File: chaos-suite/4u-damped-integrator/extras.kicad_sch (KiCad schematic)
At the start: 15 parts

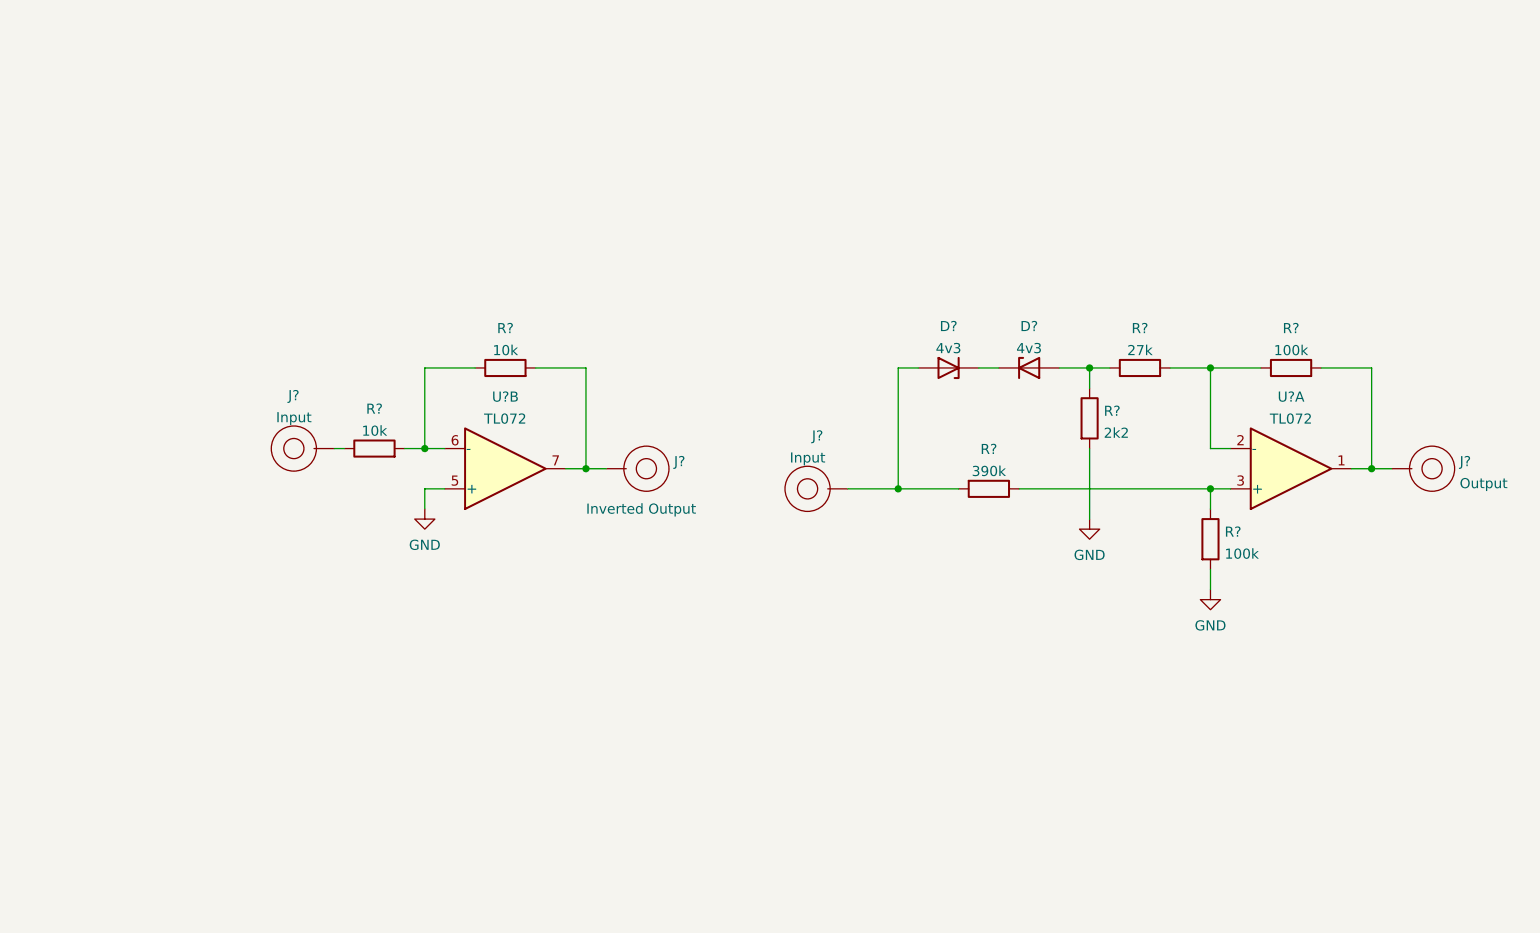
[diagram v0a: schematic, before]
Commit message: Laying out damped integrator pcb
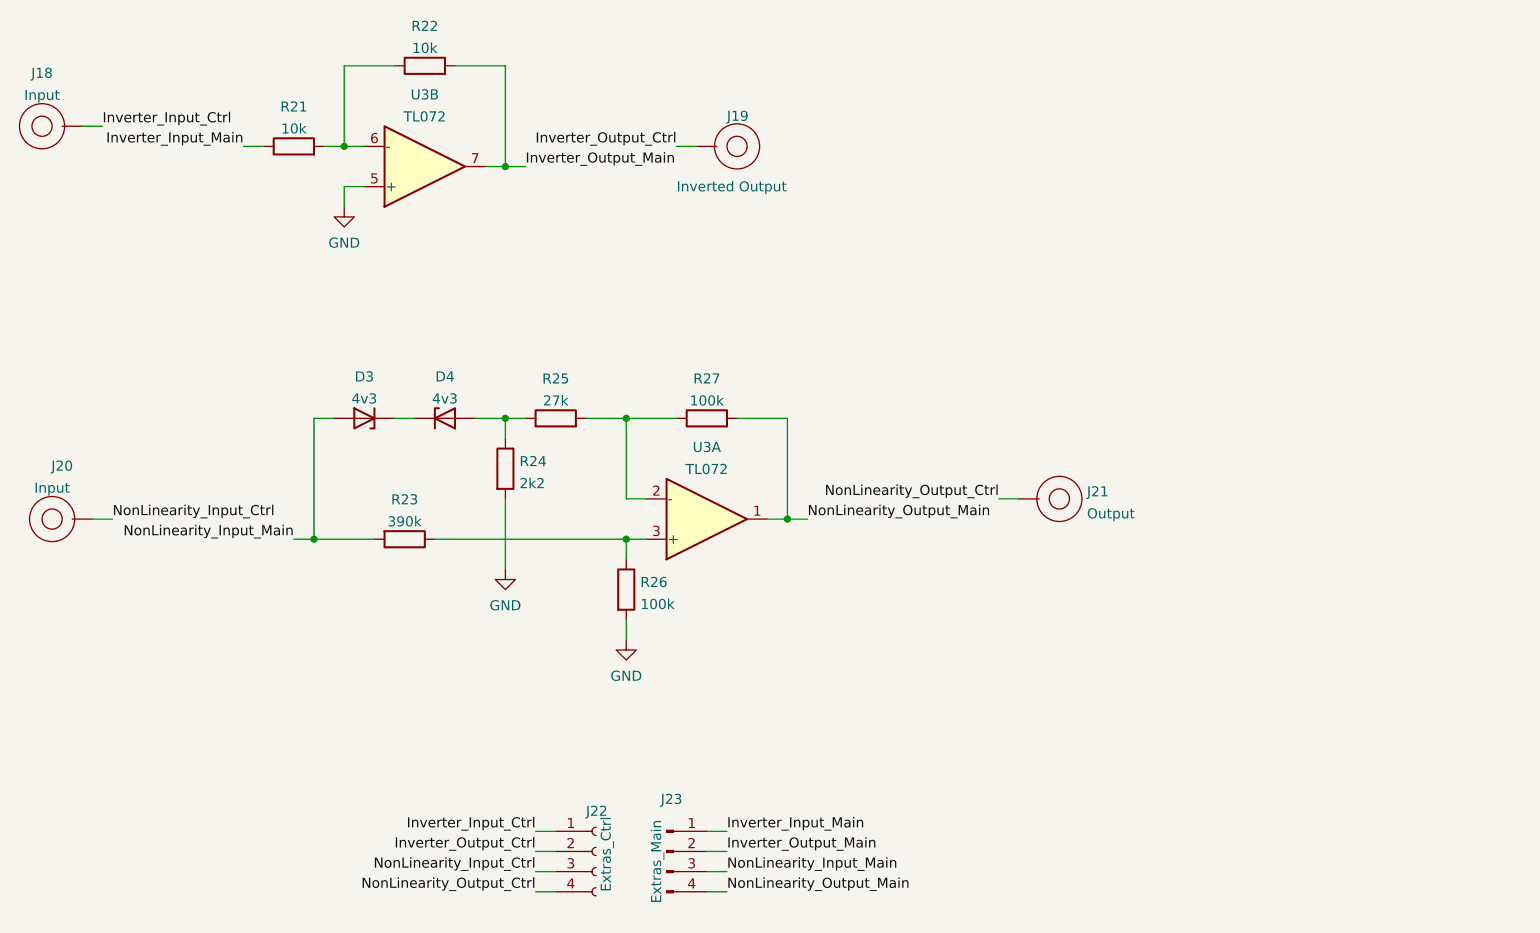
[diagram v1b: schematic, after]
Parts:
- added J22: Extras_Ctrl, Connector_PinSocket_2.54mm:PinSocket_1x04_P2.54mm_Vertical, symbol Connector:Conn_01x04_Female
- added J23: Extras_Main, Connector_PinHeader_2.54mm:PinHeader_1x04_P2.54mm_Vertical, symbol Connector:Conn_01x04_Male
- D3, D4: renamed from D?; footprint (none) -> Rumblesan_Footprints:D_DO-41_SOD81_P10.16mm_Horizontal
- J18, J19, J20, J21: renamed from J?; footprint (none) -> Rumblesan_Footprints:BananaJack_THT_JohnsonCinch_108-09
- R21, R22, R23, R24, R25, R26, R27: renamed from R?; footprint (none) -> Rumblesan_Footprints:Resistor_THT_L6.3mm_D2.5mm_P10.16mm_Horizontal
- U3: renamed from U?; footprint (none) -> Rumblesan_Footprints:DIP-8_W7.62mm_Socket
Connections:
- net Inverter_Input_Ctrl: now reaches J18.1
- net Inverter_Input_Ctrl: now also J22.1 (Pin_1); no longer R21.1
- net NonLinearity_Input_Main: now reaches D3.2 (A), R23.2
- net NonLinearity_Input_Main: now also J23.3 (Pin_3); no longer J20.1
- net NonLinearity_Output_Main: now reaches R27.2, U3.1
- net NonLinearity_Output_Main: now also J23.4 (Pin_4); no longer J21.1
- net Inverter_Output_Main: now reaches R22.2, U3.7
- net Inverter_Output_Main: now also J23.2 (Pin_2); no longer J19.1
- new net Inverter_Input_Main: J23.1 (Pin_1), R21.1
- new net Inverter_Output_Ctrl: J19.1, J22.2 (Pin_2)
- new net NonLinearity_Input_Ctrl: J20.1, J22.3 (Pin_3)
- new net NonLinearity_Output_Ctrl: J21.1, J22.4 (Pin_4)
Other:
- moved on the sheet: D3, D4, J18, J19, J20, J21, R21, R22, R23, R24, R25, R26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

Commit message: final damped integrator tweaks
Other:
- title: (none) -> Damped Integrator
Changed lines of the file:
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@@
 (kicad_sch (version 20211123) (generator eeschema)
   (paper "A4")
+  (title_block
+    (title "Damped Integrator")
+    (date "2022-06-17")
+    (rev "r01")
+    (comment 2 "creativecommons.org/Licenses/by/4.0/")
+    (comment 3 "License: CC BY 4.0")
+    (comment 4 "Author: Guy John")
+  )
   (junction (at 80.01 49.53) (diameter 0) (color 0 0 0 0)
   )

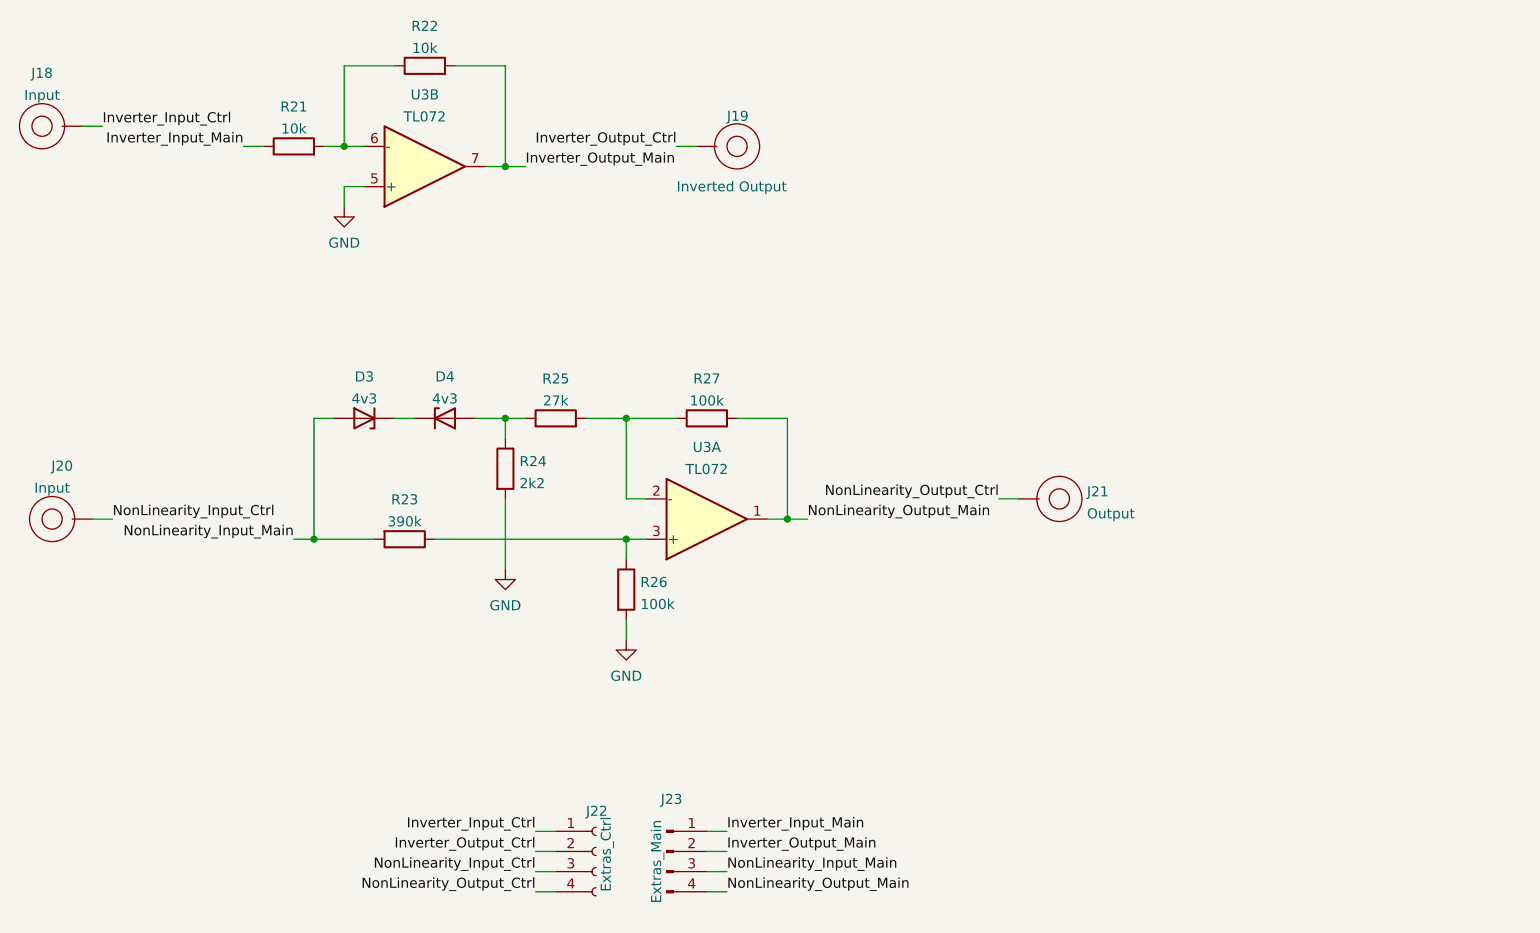
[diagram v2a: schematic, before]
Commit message: Updating damped integrator circuit and layout
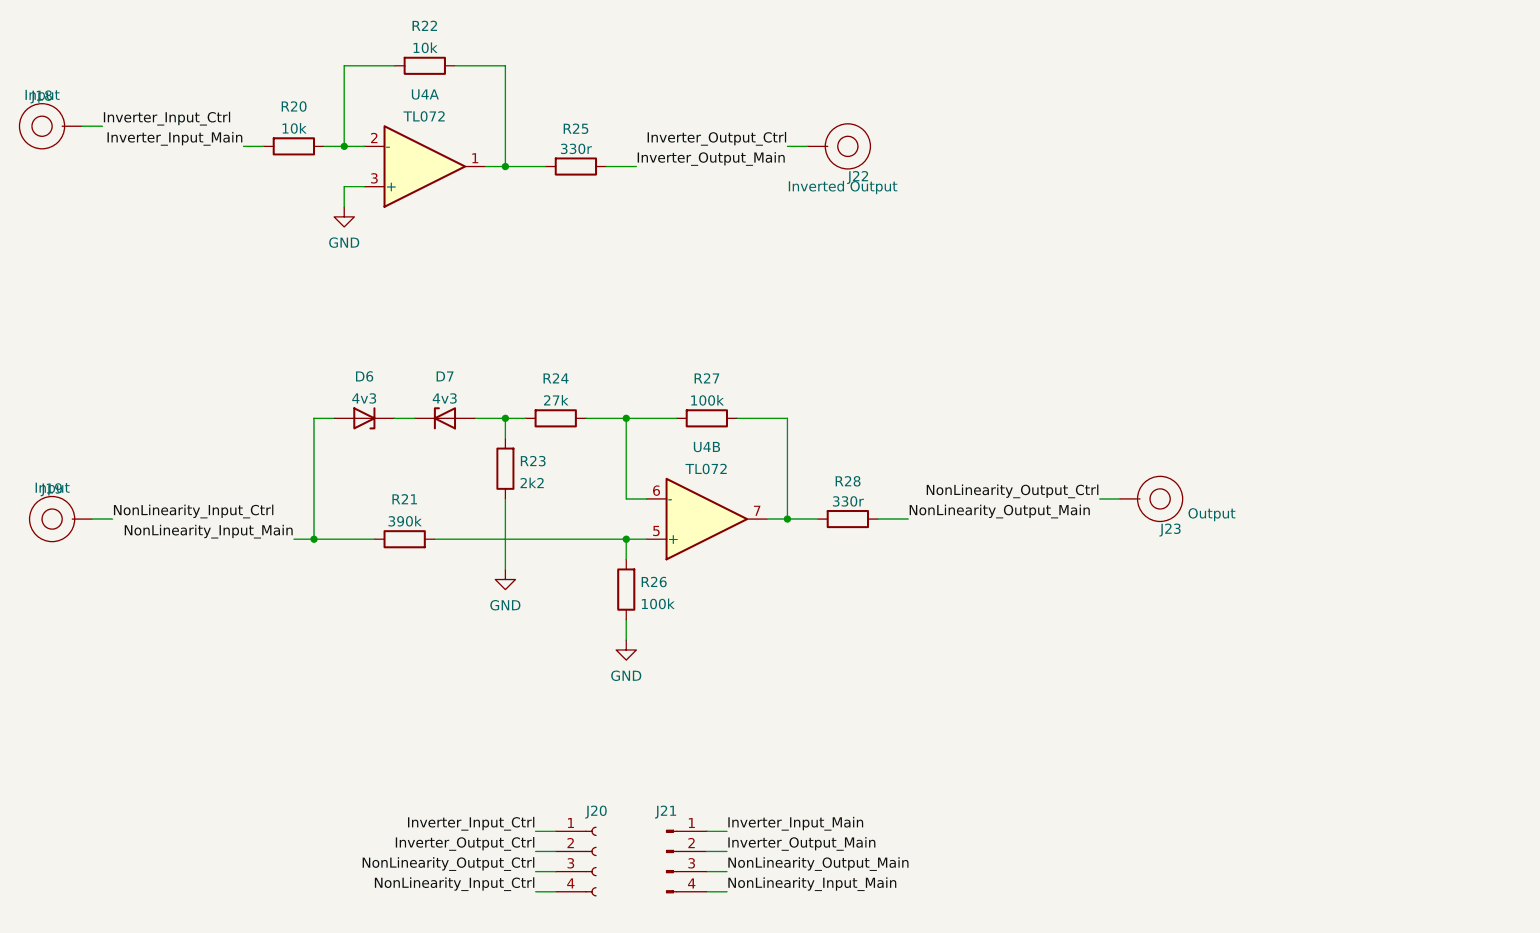
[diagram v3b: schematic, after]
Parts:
- added R25, R28: 330r, rumblesan-standard-parts:R_Axial_DIN0207_L6.3mm_D2.5mm_P10.16mm_Horizontal, symbol rumblesan-standard-parts:R
- D6: renamed from D3; footprint Rumblesan_Footprints:D_DO-41_SOD81_P10.16mm_Horizontal -> rumblesan-standard-parts:D_DO-35_SOD27_P7.62mm_Horizontal
- D7: renamed from D4; footprint Rumblesan_Footprints:D_DO-41_SOD81_P10.16mm_Horizontal -> rumblesan-standard-parts:D_DO-35_SOD27_P7.62mm_Horizontal
- J18: value BananaJack_PanelMount -> Banana Socket PanelMount; footprint Rumblesan_Footprints:BananaJack_THT_JohnsonCinch_108-09 -> rumblesan-standard-parts:BananaJack_THT_JohnsonCinch_108-09; symbol BananaJacks:BananaJack_PanelMount -> BananaJacks:Banana Socket PanelMount
- J19: renamed from J20; value BananaJack_PanelMount -> Banana Socket PanelMount; footprint Rumblesan_Footprints:BananaJack_THT_JohnsonCinch_108-09 -> rumblesan-standard-parts:BananaJack_THT_JohnsonCinch_108-09; symbol BananaJacks:BananaJack_PanelMount -> BananaJacks:Banana Socket PanelMount
- J20: renamed from J22; value Extras_Ctrl -> Conn_01x04_Female
- J21: renamed from J23; value Extras_Main -> Conn_01x04_Male
- J22: renamed from J19; value BananaJack_PanelMount -> Banana Socket PanelMount; footprint Rumblesan_Footprints:BananaJack_THT_JohnsonCinch_108-09 -> rumblesan-standard-parts:BananaJack_THT_JohnsonCinch_108-09; symbol BananaJacks:BananaJack_PanelMount -> BananaJacks:Banana Socket PanelMount
- J23: renamed from J21; value BananaJack_PanelMount -> Banana Socket PanelMount; footprint Rumblesan_Footprints:BananaJack_THT_JohnsonCinch_108-09 -> rumblesan-standard-parts:BananaJack_THT_JohnsonCinch_108-09; symbol BananaJacks:BananaJack_PanelMount -> BananaJacks:Banana Socket PanelMount
- R20: renamed from R21; footprint Rumblesan_Footprints:Resistor_THT_L6.3mm_D2.5mm_P10.16mm_Horizontal -> rumblesan-standard-parts:R_Axial_DIN0207_L6.3mm_D2.5mm_P10.16mm_Horizontal; symbol Device:R -> rumblesan-standard-parts:R; Power (none) -> 0.5W; Spec (none) -> metal film; Tolerance (none) -> 1%
- R21: renamed from R23; footprint Rumblesan_Footprints:Resistor_THT_L6.3mm_D2.5mm_P10.16mm_Horizontal -> rumblesan-standard-parts:R_Axial_DIN0207_L6.3mm_D2.5mm_P10.16mm_Horizontal; symbol Device:R -> rumblesan-standard-parts:R; Power (none) -> 0.5W; Spec (none) -> metal film; Tolerance (none) -> 1%
- R22, R26, R27: footprint Rumblesan_Footprints:Resistor_THT_L6.3mm_D2.5mm_P10.16mm_Horizontal -> rumblesan-standard-parts:R_Axial_DIN0207_L6.3mm_D2.5mm_P10.16mm_Horizontal; symbol Device:R -> rumblesan-standard-parts:R; Power (none) -> 0.5W; Spec (none) -> metal film; Tolerance (none) -> 1%
- R23: renamed from R24; footprint Rumblesan_Footprints:Resistor_THT_L6.3mm_D2.5mm_P10.16mm_Horizontal -> rumblesan-standard-parts:R_Axial_DIN0207_L6.3mm_D2.5mm_P10.16mm_Horizontal; symbol Device:R -> rumblesan-standard-parts:R; Power (none) -> 0.5W; Spec (none) -> metal film; Tolerance (none) -> 1%
- R24: renamed from R25; footprint Rumblesan_Footprints:Resistor_THT_L6.3mm_D2.5mm_P10.16mm_Horizontal -> rumblesan-standard-parts:R_Axial_DIN0207_L6.3mm_D2.5mm_P10.16mm_Horizontal; symbol Device:R -> rumblesan-standard-parts:R; Power (none) -> 0.5W; Spec (none) -> metal film; Tolerance (none) -> 1%
- U4: renamed from U3; footprint Rumblesan_Footprints:DIP-8_W7.62mm_Socket -> rumblesan-standard-parts:DIP-8_W7.62mm_Socket
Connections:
- net GND: now also R23.1, R26.1, U4.3 (+); no longer R23.2, R26.2, U4.5 (+)
- net Inverter_Input_Main: now also R20.2; no longer R20.1
- net Inverter_Output_Main: now also R25.1; no longer R22.2, U4.7
- net NonLinearity_Input_Ctrl: now also J20.4 (Pin_4); no longer J20.3 (Pin_3)
- net NonLinearity_Input_Main: now also J21.4 (Pin_4), R21.1; no longer J21.3 (Pin_3), R21.2
- net NonLinearity_Output_Ctrl: now also J20.3 (Pin_3); no longer J20.4 (Pin_4)
- net NonLinearity_Output_Main: now also J21.3 (Pin_3), R28.1; no longer J21.4 (Pin_4), R27.2, U4.1
- new net: D7.2 (A), R23.2, R24.2
- new net: R20.1, R22.2, U4.2 (-)
- new net: R22.1, R25.2, U4.1
- new net: R24.1, R27.2, U4.6 (-)
- new net: R21.2, R26.2, U4.5 (+)
- new net: R27.1, R28.2, U4.7
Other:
- moved on the sheet: J22, J23, U4A, U4B
